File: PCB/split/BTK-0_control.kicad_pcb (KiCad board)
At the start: 4 copper layers, 22 x 51.5 mm, 27 parts, among them J1 USB_C_Receptacle_USB2.0_16P, J6 Conn_01x16_Pin, SW1 EN, SW2 BOOT, U1 NCP1117-3.3_SOT223, U2 NCP1117-3.3_SOT223, U3 USBLC6-2SC6, U4 ESP32-C6-MINI-1, U5 TVS1400DRV

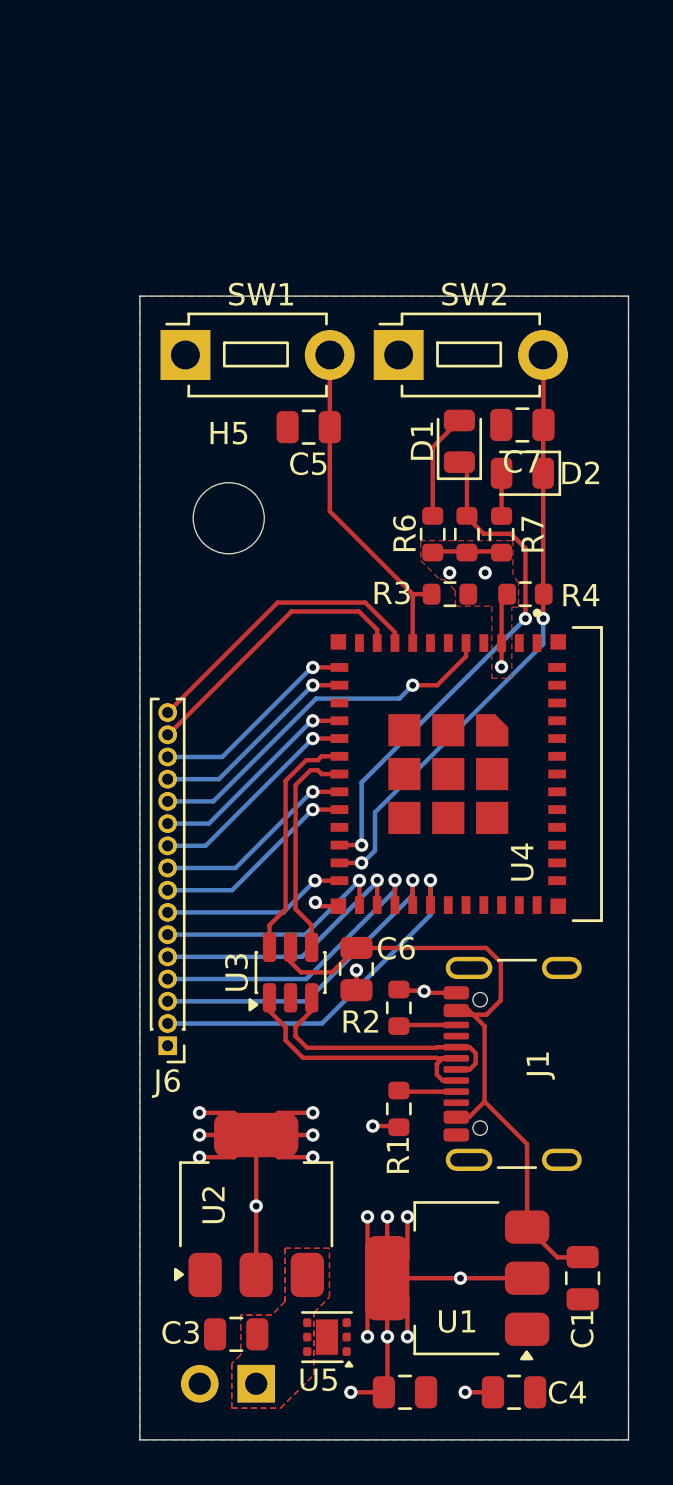
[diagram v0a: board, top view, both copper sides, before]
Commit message: re-centered control cad
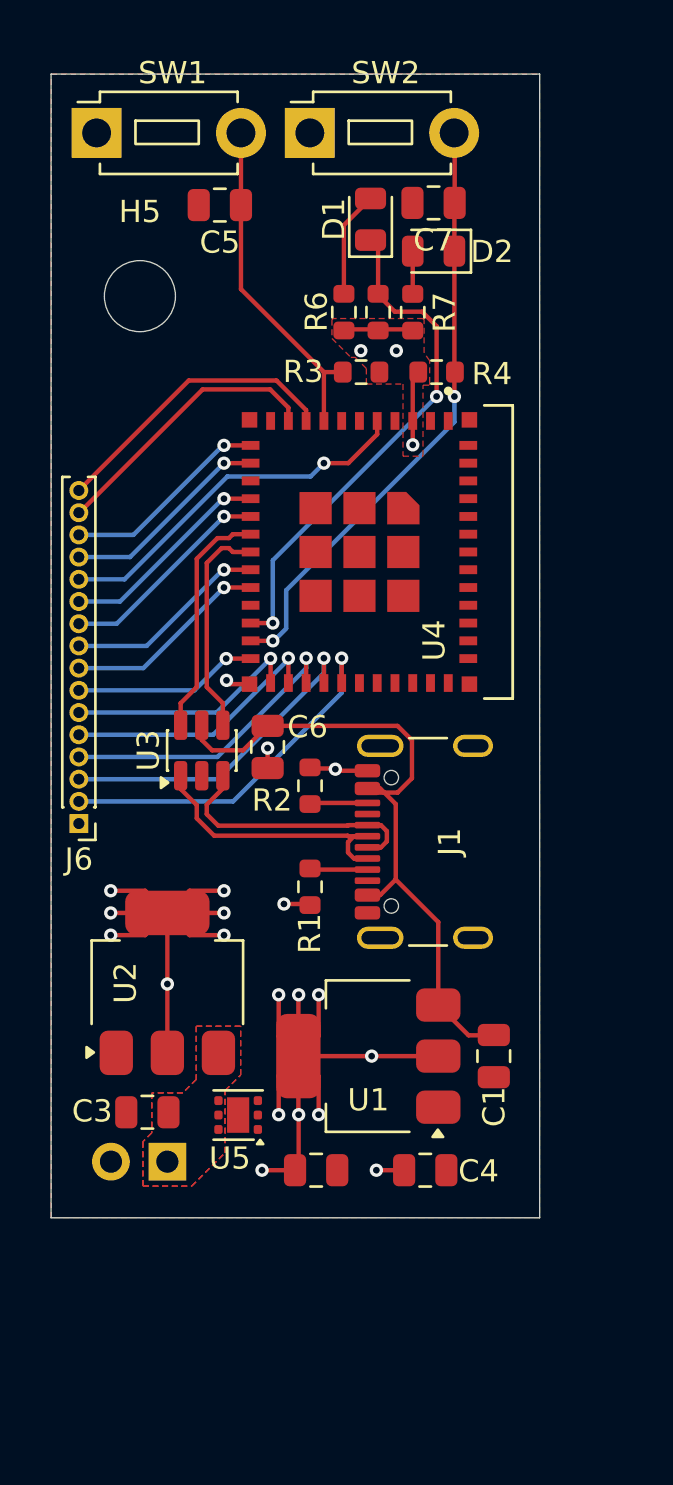
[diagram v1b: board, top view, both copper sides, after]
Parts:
- moved U2 10.8 mm to (1.24, 30.9)
- moved BT1 10.8 mm to (1.24, 39.0)
- moved C2 10.8 mm to (7.93, 39.4)
- moved C4 10.8 mm to (12.8, 39.4)
- moved C6 10.8 mm to (5.75, 20.3)
- moved C7 10.8 mm to (13.2, -4.20)
- moved D1 10.8 mm to (10.4, -3.46)
- moved D2 10.8 mm to (13.2, -2.02)
- moved H5 10.8 mm to (0.00, 0.00)
- moved J1 10.8 mm to (13.9, 24.6)
- moved J6 10.8 mm to (-2.75, 23.8)
- moved R1 10.8 mm to (7.66, 26.6)
- moved R2 10.8 mm to (7.66, 22.0)
- moved R3 10.8 mm to (9.96, 3.42)
- moved R4 10.8 mm to (13.4, 3.42)
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
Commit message: im boutta die son
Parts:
- moved C1 0.37 mm to (15.7, 34.0)
- moved C4 0.37 mm to (12.6, 39.1)
- moved C6 0.37 mm to (5.47, 20.1)
- moved C7 0.37 mm to (12.9, -4.45)
- moved D1 0.37 mm to (10.1, -3.71)
- moved D2 0.37 mm to (12.9, -2.27)
- moved J1 0.37 mm to (13.7, 24.3)
- moved R1 0.37 mm to (7.38, 26.3)
- moved R2 0.37 mm to (7.38, 21.8)
- moved R3 0.37 mm to (9.69, 3.17)
- moved R5 0.37 mm to (10.4, 0.47)
- moved R6 0.37 mm to (8.91, 0.47)
- moved R7 0.37 mm to (12.0, 0.48)
- moved SW2 0.37 mm to (7.38, -7.60)
- moved U1 0.37 mm to (10.0, 34.0)
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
